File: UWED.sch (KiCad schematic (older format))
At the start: 52 parts, among them U1 RFD22301

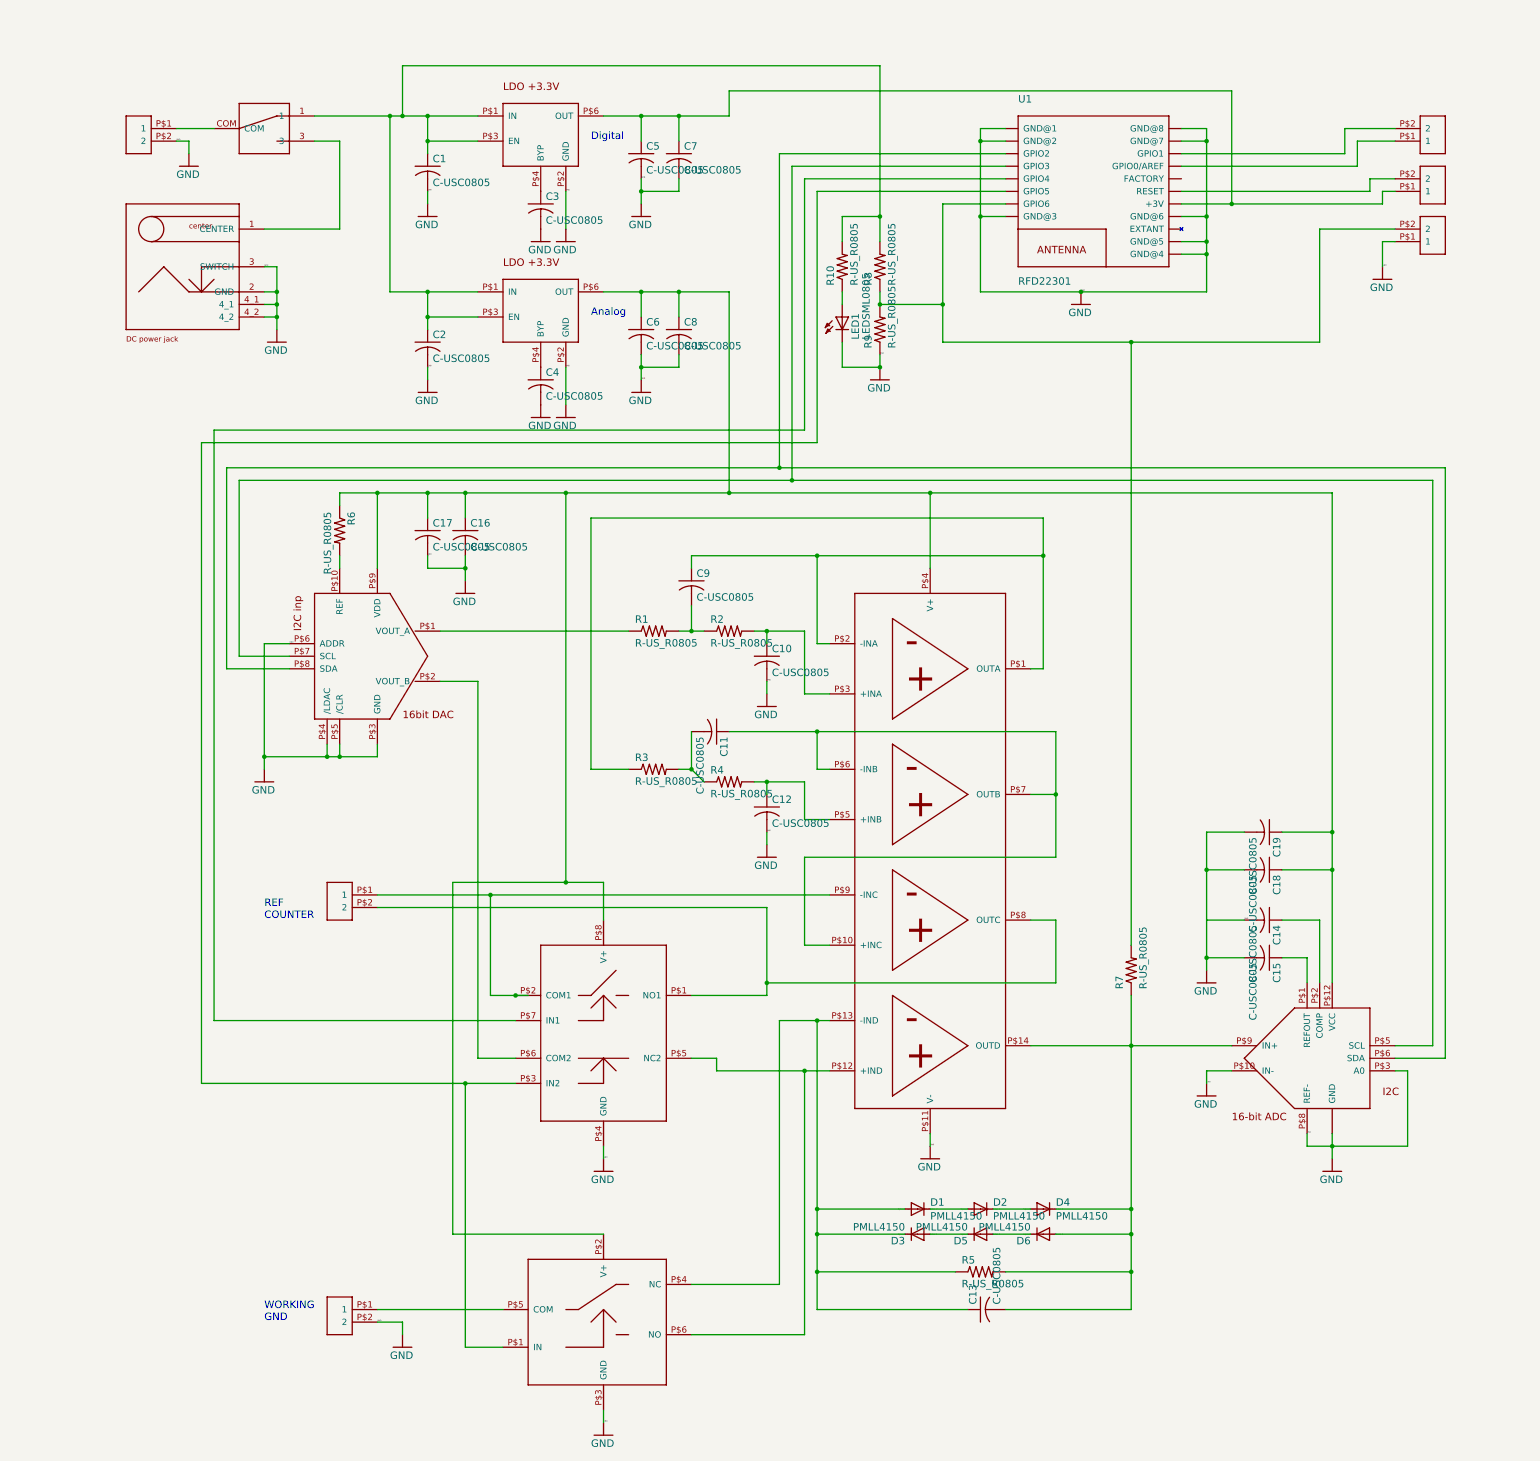
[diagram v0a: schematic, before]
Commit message: New project files with ESP-WROOM-32 and integrated charger chip - untested.
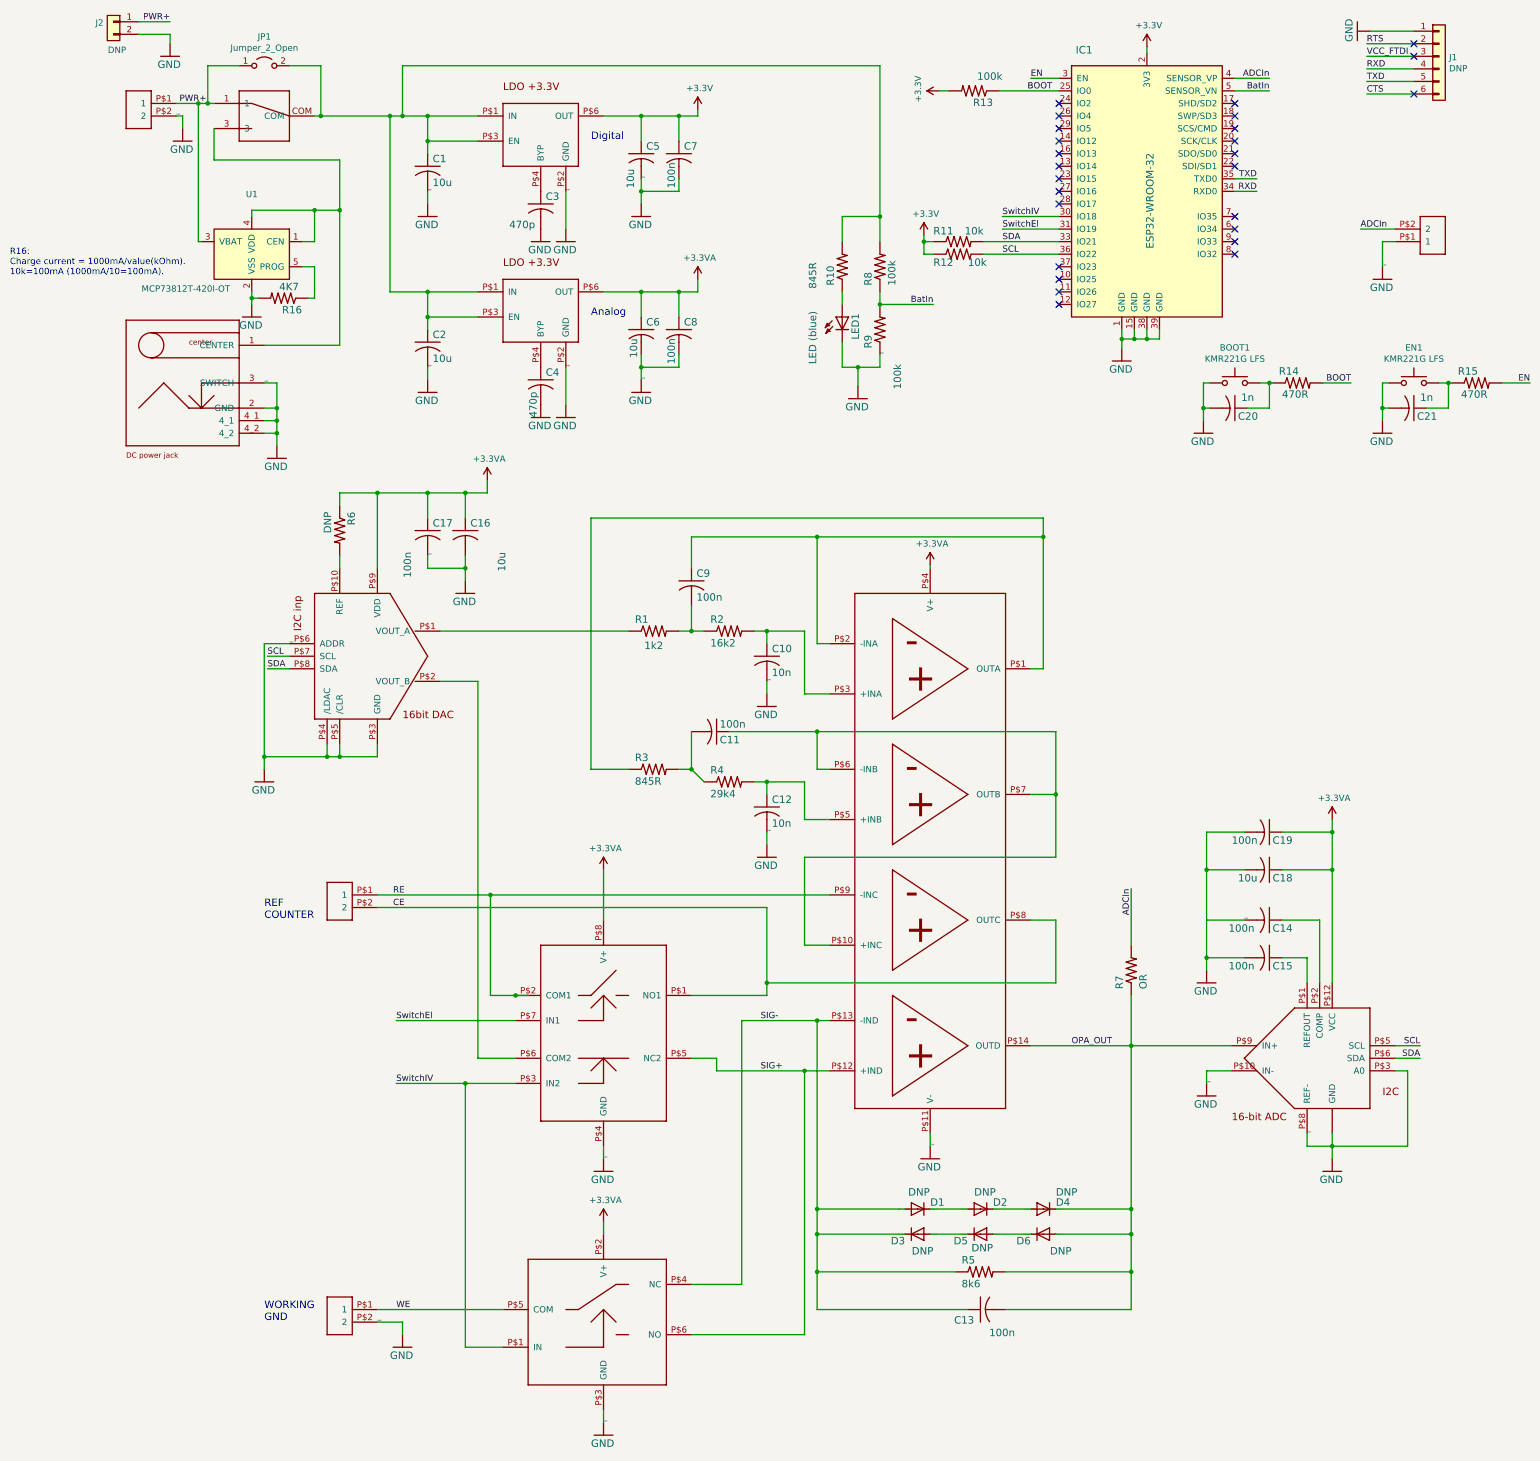
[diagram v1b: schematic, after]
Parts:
- removed U$4, U$5: CONTACT_PADS_SMD_2, UWED:CONTACT_PADS_SMD_2, symbol UWED-eagle-import:CONTACT_PADS_SMD_2
- removed U1: RFD22301, UWED:RFD22301, symbol UWED-eagle-import:RFD22301
- added BOOT1, EN1: KMR221G LFS, Buttons_Switches_SMD:SW_SPST_KMR2, symbol Switch:SW_Push
- added C20, C21: 1n, UWED:C0805, symbol UWED-eagle-import:C-USC0805
- added IC1: ESP32-WROOM-32, digikey-footprints:ESP32-WROOM-32D, symbol dk_RF-Transceiver-Modules:ESP32-WROOM-32
- added J1: DNP, Pin_Headers:Pin_Header_Straight_1x06_Pitch2.54mm, symbol Connector_Generic:Conn_01x06
- added J2: DNP, Pin_Headers:Pin_Header_Straight_1x02_Pitch2.54mm, symbol Connector_Generic:Conn_01x02
- added JP1: Jumper_2_Open, Jumper:SolderJumper-2_P1.3mm_Open_TrianglePad1.0x1.5mm, symbol Jumper:Jumper_2_Open
- added R11, R12: 10k, UWED:R0805, symbol UWED-eagle-import:R-US_R0805
- added R13: 100k, UWED:R0805, symbol UWED-eagle-import:R-US_R0805
- added R14, R15: 470R, UWED:R0805, symbol UWED-eagle-import:R-US_R0805
- added R16: 4K7, UWED:R0805, symbol UWED-eagle-import:R-US_R0805
- added U1: MCP73812T-420I-OT, TO_SOT_Packages_SMD:SOT-23-5_HandSoldering, symbol Battery_Management:MCP73812T-420I-OT
- C1, C2: value C-USC0805 -> 10u; Description (none) -> LDO input cap; desc (none) -> CAP 10u 0805; digikey.manf# (none) -> 490-3340-1-ND; manf (none) -> Murata Electronics; manf# (none) -> GRM219R60J106KE19D
- C10, C12: value C-USC0805 -> 10n; Description (none) -> Filter cap.; Manufacturer (none) -> Yageo; desc (none) -> CAP 10n 0805; digikey.manf# (none) -> 311-1136-1-ND; manf# (none) -> CC0805KRX7R9BB103
- C11, C9: value C-USC0805 -> 100n; Description (none) -> Filter cap.; desc (none) -> CAP 100n 0805; digikey.manf# (none) -> 478-1395-1-ND; manf (none) -> AVX Corporation; manf# (none) -> 08055C104KAT2A
- C13: value C-USC0805 -> 100n; Description (none) -> WE aplifier cap; desc (none) -> CAP 100n 0805; digikey.manf# (none) -> 478-1395-1-ND; manf (none) -> AVX Corporation; manf# (none) -> 08055C104KAT2A
- C14, C15: value C-USC0805 -> 100n; Description (none) -> Ext ADC cap.; desc (none) -> CAP 100n 0805; digikey.manf# (none) -> 478-1395-1-ND; manf (none) -> AVX Corporation; manf# (none) -> 08055C104KAT2A
- C16: value C-USC0805 -> 10u; Description (none) -> DAC power cap.; desc (none) -> CAP 10u 0805; digikey.manf# (none) -> 490-3340-1-ND; manf (none) -> Murata Electronics; manf# (none) -> GRM219R60J106KE19D
- C17: value C-USC0805 -> 100n; Description (none) -> DAC power cap.; desc (none) -> CAP 100n 0805; digikey.manf# (none) -> 478-1395-1-ND; manf (none) -> AVX Corporation; manf# (none) -> 08055C104KAT2A
- C18: value C-USC0805 -> 10u; Description (none) -> ADC power cap.; desc (none) -> CAP 10u 0805; digikey.manf# (none) -> 490-3340-1-ND; manf (none) -> Murata Electronics; manf# (none) -> GRM219R60J106KE19D
- C19: value C-USC0805 -> 100n; Description (none) -> ADC power cap; desc (none) -> CAP 100n 0805; digikey.manf# (none) -> 478-1395-1-ND; manf (none) -> AVX Corporation; manf# (none) -> 08055C104KAT2A
- C3, C4: value C-USC0805 -> 470p; Description (none) -> LDO cap.; desc (none) -> CAP 470p 0805; digikey.manf# (none) -> 1276-1300-1-ND; manf (none) -> Samsung Electro-Mechanics; manf# (none) -> CL21B471KBANNNC
- C5, C6: value C-USC0805 -> 10u; Description (none) -> LDO output cap; desc (none) -> CAP 10u 0805; digikey.manf# (none) -> 490-3340-1-ND; manf (none) -> Murata Electronics; manf# (none) -> GRM219R60J106KE19D
- C7, C8: value C-USC0805 -> 100n; Description (none) -> LDO output cap; desc (none) -> CAP 100n 0805; digikey.manf# (none) -> 478-1395-1-ND; manf (none) -> AVX Corporation; manf# (none) -> 08055C104KAT2A
- D1, D2, D3, D4, D5, D6: value PMLL4150 -> DNP; Description (none) -> PMLL4150; desc (none) -> DNP Log Diode; dnp (none) -> 1; manf (none) -> NXP Semiconductors; manf# (none) -> PMLL4150
- IC2: renamed from U$8; Description (none) -> Dual DAC. 16-bit I2C; MPN (none) -> AD5667RBRMZ-2; desc (none) -> Dual DAC. 16-bit I2C; digikey.manf# (none) -> AD5667RBRMZ-2-ND; manf (none) -> Analog Devices; manf# (none) -> AD5667RBRMZ-2
- IC3: renamed from U$1; Description (none) -> 4x oparetional amplifiers; MPN (none) -> AD8608ARUZ; desc (none) -> QUAD OPAMP; digikey.manf# (none) -> AD868ARUZ-ND; manf (none) -> Analog Devices; manf# (none) -> AD8608ARUZ
- IC4: renamed from U$10; Description (none) -> LDO 3V3; MPN (none) -> MIC5205-3.3YM5-TR; desc (none) -> LDO 3V3; digikey.manf# (none) -> 576-1259-1-ND; manf (none) -> Micron; manf# (none) -> MIC5205-3.3YM5-TR
- IC5: renamed from U$11; Description (none) -> LDO 3V3; MPN (none) -> MIC5205-3.3YM5-TR; desc (none) -> LDO 3V3; digikey.manf# (none) -> 576-1259-1-ND; manf (none) -> Micron; manf# (none) -> MIC5205-3.3YM5-TR
- IC6: renamed from U$12; Description (none) -> Dual switch; MPN (none) -> MAX4643EUA+; desc (none) -> Dual switch; digikey.manf# (none) -> MAX4643EUA+-ND; manf (none) -> Maxim; manf# (none) -> MAX4643EUA+
- IC7: renamed from U$13; Description (none) -> Single switch; MPN (none) -> MAX4644EUT+T; desc (none) -> Single switch; digikey.manf# (none) -> MAX4644EUT+TCTND; manf (none) -> Maxim; manf# (none) -> MAX4644EUT+T
- IC8: renamed from U$2; Description (none) -> 16-bit ADC, I2C; MPN (none) -> LTC2471IMS#PBF; desc (none) -> 16-bit ADC, I2C; digikey.manf# (none) -> LTC2471IMS#PBFND; manf (none) -> Analog Devices; manf# (none) -> LTC2471IMS#PBF
- LED1: value LEDSML0805 -> LED (blue); desc (none) -> Led Blue Clear 0805; digikey.manf# (none) -> VAOL-S8SB4CT-ND; manf (none) -> Visual Communications Company - VCC; manf# (none) -> VAOL-S8SB4
- P1: renamed from U$9; value DC_JACK_0.7MM -> PJ-032H-SMT-TR; Description (none) -> Jack 0.7x2.35mm; MPN (none) -> PJ-032H-SMT-TR; desc (none) -> Jack 0.7x2.35mm; digikey.manf# (none) -> CP-032HPJCT-ND; manf (none) -> CUI Inc.; manf# (none) -> PJ-032H-SMT-TR
- P2: renamed from U$14; value SW_TOGGLELARGE -> 34EWMSP12M6RT; Description (none) -> Power switch; MPN (none) -> 34EWMSP12M6RT; desc (none) -> Toggle Switch SPDT Surface Mount, Right Angle; digikey.manf# (none) -> GH7540CT-ND; manf (none) -> Grayhill Inc.; manf# (none) -> 34EWMSP12M6RT
- R1: value R-US_R0805 -> 1k2; Description (none) -> RES 1K2 0806; desc (none) -> RES 1K2 0806; digikey.manf# (none) -> RR12P1.2KDCT-ND; manf (none) -> Susumu; manf# (none) -> RR1220P-122-D
- R10, R3: value R-US_R0805 -> 845R; Description (none) -> RES 845R 0806; desc (none) -> RES 845R 0806; digikey.manf# (none) -> 311-845CRCT-ND; manf (none) -> Yageo; manf# (none) -> RC0805FR-07845RL
- R2: value R-US_R0805 -> 16k2; Description (none) -> RES 16K2 0806; desc (none) -> RES 16K2 0806; digikey.manf# (none) -> 311-16.2KCRCT-ND; manf (none) -> Yageo; manf# (none) -> RC0805FR-0716K2L
- R4: value R-US_R0805 -> 29k4; Description (none) -> RES 29K4 0806; desc (none) -> RES 29K4 0806; digikey.manf# (none) -> 311-29.4KCRCT-ND; manf (none) -> Yageo; manf# (none) -> RC0805FR-0729K4L
- R5: value R-US_R0805 -> 8k6; desc (none) -> RES 8K06 0806; digikey.manf# (none) -> 311-8.06KCRCT-ND; manf (none) -> Yageo; manf# (none) -> RC0805FR-078K06L
- R6: value R-US_R0805 -> DNP; Description (none) -> RES 0R 0806; desc (none) -> RES 0R 0806; digikey.manf# (none) -> 541-4126-1-ND; dnp (none) -> 1; manf (none) -> Vishay Dale; manf# (none) -> CRCW08050000Z0EBC
- R7: value R-US_R0805 -> OR; Description (none) -> RES 0R 0806; desc (none) -> RES 0R 0806; digikey.manf# (none) -> 541-4126-1-ND; manf (none) -> Vishay Dale; manf# (none) -> CRCW08050000Z0EBC
- R8, R9: value R-US_R0805 -> 100k; Description (none) -> RES 100K 0806; desc (none) -> RES 100K 0806; digikey.manf# (none) -> 541-4164-1-ND; manf (none) -> Vishay Dale; manf# (none) -> CRCW0805100KJNEAC
- U$15, U$3, U$6, U$7: dnp (none) -> 1
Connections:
- net +3.3VA: now reaches C16.1, C17.1, C18.1, C19.1, C6.1, C8.1, IC2.P$9 (VDD), IC3.P$4 (V+), IC5.P$6 (OUT), IC6.P$8 (V+), IC7.P$2 (V+), IC8.P$12 (VCC), R6.1
- net at C1.1, C2.1, IC4.P$1 (IN)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: now also P2.COM, JP1.2 (B); no longer P2.1
- net ADCIn: now reaches R7.2, U$15.P$2 (2)
- net ADCIn: now also IC1.4 (SENSOR_VP); no longer R8.1, R9.2
- net +3V3: now reaches C5.1, C7.1, IC4.P$6 (OUT)
- net +3V3: now also IC1.2 (3V3), R11.1, R12.1, R13.2
- net SwitchIV: now reaches IC6.P$3 (IN2), IC7.P$1 (IN)
- net SwitchIV: now also IC1.30 (IO18)
- net SIG-: now reaches C13.1, D1.A, D3.C, IC3.P$13 (-IND), IC7.P$4 (NC), R5.1
- net WE: now reaches IC7.P$5 (COM), U$6.P$1 (1)
- net SIG+: now reaches IC3.P$12 (+IND), IC6.P$5 (NC2), IC7.P$6 (NO)
- net OPA_OUT: now reaches C13.2, D4.C, D6.A, IC3.P$14 (OUTD), IC8.P$9 (IN+), R5.2, R7.1
- net SCL: now reaches IC2.P$7 (SCL), IC8.P$5 (SCL)
- net SCL: now also IC1.36 (IO22), R12.2
- net SDA: now reaches IC2.P$8 (SDA), IC8.P$6 (SDA)
- net SDA: now also IC1.33 (IO21), R11.2
- net RE: now reaches IC3.P$9 (-INC), IC6.P$2 (COM1), U$7.P$1 (1)
- net CE: now reaches IC3.P$8 (OUTC), IC6.P$1 (NO1), U$7.P$2 (2)
- net PWR+: now reaches U$3.P$1 (1)
- net PWR+: now also P2.1, J2.1 (Pin_1), JP1.1 (A), U1.3 (VBAT); no longer P2.COM
- net SwitchEl: now reaches IC6.P$7 (IN1)
- net SwitchEl: now also IC1.31 (IO19)
- net at P1.1 (CENTER), P2.3: now also U1.1 (CEN), U1.4 (VDD)
- new net: IC1.1 (GND), IC1.15 (GND), IC1.38 (GND), IC1.39 (GND)
- new net: R16.2, U1.2 (VSS)
- new net: R16.1, U1.5 (PROG)
- new net: BOOT1.2, C20.1, R14.1
- new net: BOOT1.1, C20.2
- new net: C21.1, EN1.2, R15.1
- new net: C21.2, EN1.1
- new net BOOT: IC1.25 (IO0), R13.1, R14.2
- new net BatIn: IC1.5 (SENSOR_VN), R8.1, R9.2
- new net CTS: J1.6 (Pin_6)
- new net EN: IC1.3 (EN), R15.2
- new net RTS: J1.2 (Pin_2)
- new net RXD: IC1.34 (RXD0), J1.4 (Pin_4)
- new net TXD: IC1.35 (TXD0), J1.5 (Pin_5)
- new net VCC_FTDI: J1.3 (Pin_3)
- no-connect marks 0 -> 26
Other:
- note added: "R16:\nCharge current = 1000mA/value(kOhm).\n10k=100mA (1000mA/10=100mA)."
